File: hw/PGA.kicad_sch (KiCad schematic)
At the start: 17 parts, among them U1401 MAX9939AUB+T

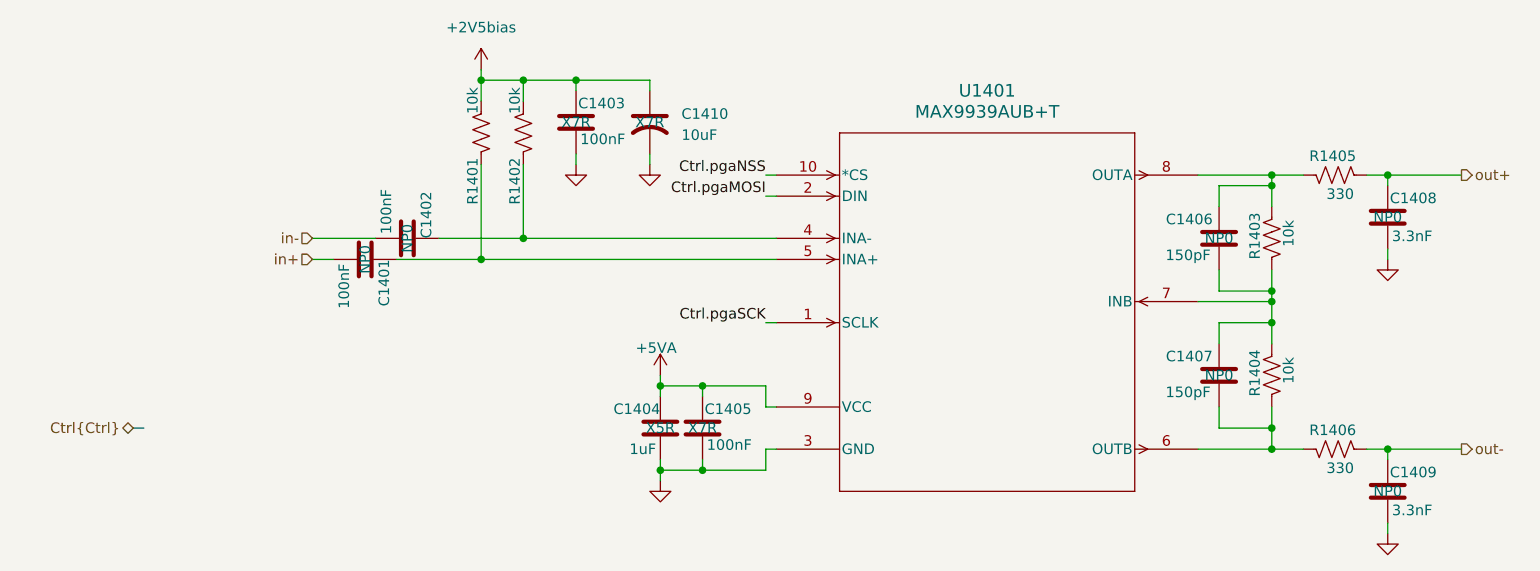
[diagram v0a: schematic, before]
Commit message: Added support for four audio serial links from AK5578 codec to STM32H753, each with 22 ohm series R and I put series R in the clock outputs from STM32 toward AK5578 as well. Reannotated.
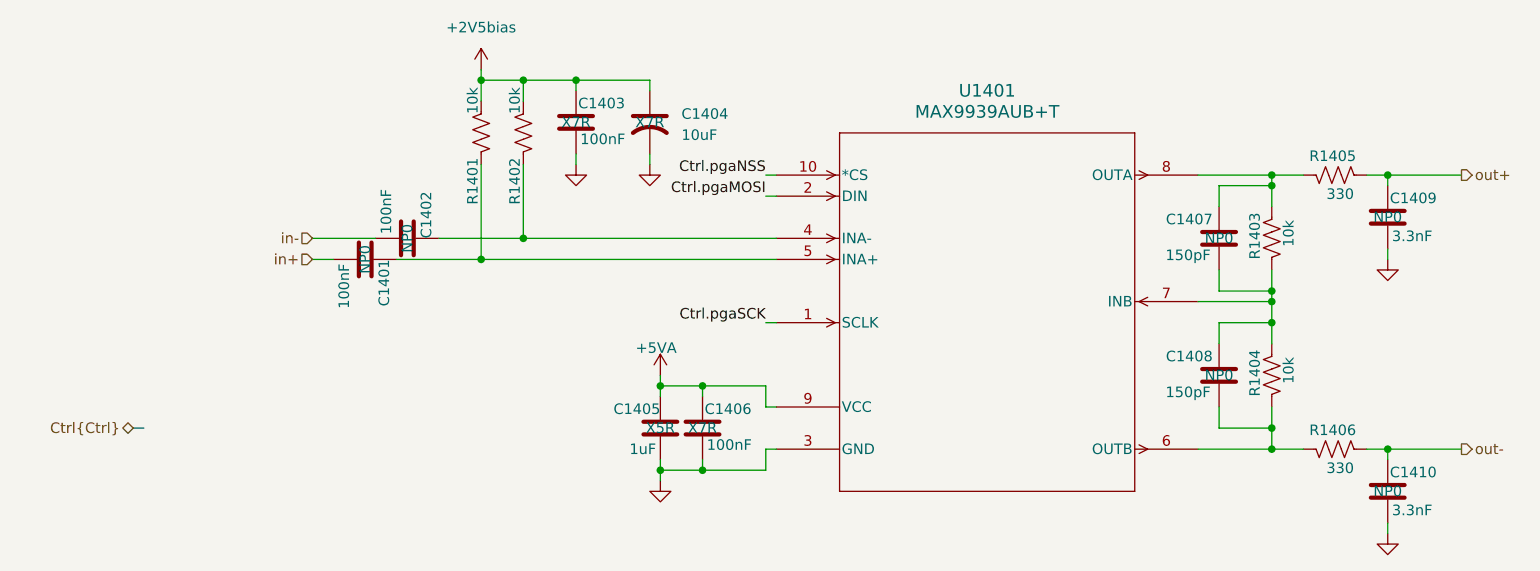
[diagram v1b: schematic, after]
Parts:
- renumbered C1410 to C1404, C1404 to C1405, C1405 to C1406, C1406 to C1407, C1407 to C1408, C1408 to C1409, C1409 to C1410

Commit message: Checkpoint before crazy script screws my files up (again)
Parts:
- renumbered C1401 to C1405, C1402 to C1407, C1403 to C1410, C1404 to C1411, C1405 to C1412, C1406 to C1413, C1407 to C1418, C1408 to C1419, C1409 to C1422, C1410 to C1423, R1401 to R1402, R1402 to R1405, R1403 to R1411, R1404 to R1412, R1405 to R1413, R1406 to R1414
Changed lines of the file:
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@@
 		(on_board yes)
 		(dnp no)
-		(property "Reference" "R1403"
+		(property "Reference" "R1411"
 			(at 164.338 78.74 90)
 			(effects
@@
 				)
 				(path "/8ae46c04-d01a-4756-8774-512b694bfaff/0ee31834-a2c3-474b-9f7c-c9b4f3cadb3f/104f4ab4-5f9d-46b7-aa11-a9b548b73874/5ffcf0e7-51e5-47a9-8fef-78cb8699aff9"
-					(reference "R1403")
+					(reference "R1411")
 					(unit 1)
 				)
@@
 		(on_board yes)
 		(dnp no)
-		(property "Reference" "C1409"
+		(property "Reference" "C1422"
 			(at 180.594 71.374 0)
 			(effects
@@
 				)
 				(path "/8ae46c04-d01a-4756-8774-512b694bfaff/0ee31834-a2c3-474b-9f7c-c9b4f3cadb3f/104f4ab4-5f9d-46b7-aa11-a9b548b73874/5ffcf0e7-51e5-47a9-8fef-78cb8699aff9"
-					(reference "C1409")
+					(reference "C1422")
 					(unit 1)
 				)
@@
 		(on_board yes)
 		(dnp no)
-		(property "Reference" "R1406"
+		(property "Reference" "R1414"
 			(at 176.53 99.314 90)
 			(effects
@@
 				)
 				(path "/8ae46c04-d01a-4756-8774-512b694bfaff/0ee31834-a2c3-474b-9f7c-c9b4f3cadb3f/104f4ab4-5f9d-46b7-aa11-a9b548b73874/5ffcf0e7-51e5-47a9-8fef-78cb8699aff9"
-					(reference "R1406")
+					(reference "R1414")
 					(unit 1)
 				)
@@
 		(dnp no)
 		(fields_autoplaced yes)
-		(property "Reference" "#PWR01405"
+		(property "Reference" "#PWR01417"
 			(at 92.71 111.76 0)
 			(effects
@@
 				)
 				(path "/8ae46c04-d01a-4756-8774-512b694bfaff/0ee31834-a2c3-474b-9f7c-c9b4f3cadb3f/104f4ab4-5f9d-46b7-aa11-a9b548b73874/5ffcf0e7-51e5-47a9-8fef-78cb8699aff9"
-					(reference "#PWR01405")
+					(reference "#PWR01417")
 					(unit 1)
 				)
@@
 		(on_board yes)
 		(dnp no)
-		(property "Reference" "C1407"
+		(property "Reference" "C1418"
 			(at 159.258 73.914 0)
 			(effects
@@
 				)
 				(path "/8ae46c04-d01a-4756-8774-512b694bfaff/0ee31834-a2c3-474b-9f7c-c9b4f3cadb3f/104f4ab4-5f9d-46b7-aa11-a9b548b73874/5ffcf0e7-51e5-47a9-8fef-78cb8699aff9"
-					(reference "C1407")
+					(reference "C1418")
 					(unit 1)
 				)
@@
 		(on_board yes)
 		(dnp no)
-		(property "Reference" "C1408"
+		(property "Reference" "C1419"
 			(at 159.258 90.424 0)
 			(effects
@@
 				)
 				(path "/8ae46c04-d01a-4756-8774-512b694bfaff/0ee31834-a2c3-474b-9f7c-c9b4f3cadb3f/104f4ab4-5f9d-46b7-aa11-a9b548b73874/5ffcf0e7-51e5-47a9-8fef-78cb8699aff9"
-					(reference "C1408")
+					(reference "C1419")
 					(unit 1)
 				)
@@
 		(on_board yes)
 		(dnp no)
-		(property "Reference" "C1410"
+		(property "Reference" "C1423"
 			(at 180.594 104.394 0)
 			(effects
@@
 				)
 				(path "/8ae46c04-d01a-4756-8774-512b694bfaff/0ee31834-a2c3-474b-9f7c-c9b4f3cadb3f/104f4ab4-5f9d-46b7-aa11-a9b548b73874/5ffcf0e7-51e5-47a9-8fef-78cb8699aff9"
-					(reference "C1410")
+					(reference "C1423")
 					(unit 1)
 				)
@@
 		(on_board yes)
 		(dnp no)
-		(property "Reference" "R1401"
+		(property "Reference" "R1402"
 			(at 70.104 72.136 90)
 			(effects
@@
 				)
 				(path "/8ae46c04-d01a-4756-8774-512b694bfaff/0ee31834-a2c3-474b-9f7c-c9b4f3cadb3f/104f4ab4-5f9d-46b7-aa11-a9b548b73874/5ffcf0e7-51e5-47a9-8fef-78cb8699aff9"
-					(reference "R1401")
+					(reference "R1402")
 					(unit 1)
 				)
@@
 		(dnp no)
 		(fields_autoplaced yes)
-		(property "Reference" "#PWR01401"
+		(property "Reference" "#PWR01411"
 			(at 71.12 59.69 0)
 			(effects
@@
 				)
 				(path "/8ae46c04-d01a-4756-8774-512b694bfaff/0ee31834-a2c3-474b-9f7c-c9b4f3cadb3f/104f4ab4-5f9d-46b7-aa11-a9b548b73874/5ffcf0e7-51e5-47a9-8fef-78cb8699aff9"
-					(reference "#PWR01401")
+					(reference "#PWR01411")
 					(unit 1)
 				)
@@
 		(dnp no)
 		(fields_autoplaced yes)
-		(property "Reference" "#PWR01403"
+		(property "Reference" "#PWR01415"
 			(at 91.44 73.66 0)
 			(effects
@@
 				)
 				(path "/8ae46c04-d01a-4756-8774-512b694bfaff/0ee31834-a2c3-474b-9f7c-c9b4f3cadb3f/104f4ab4-5f9d-46b7-aa11-a9b548b73874/5ffcf0e7-51e5-47a9-8fef-78cb8699aff9"
-					(reference "#PWR01403")
+					(reference "#PWR01415")
 					(unit 1)
 				)
@@
 		(on_board yes)
 		(dnp no)
-		(property "Reference" "R1404"
+		(property "Reference" "R1412"
 			(at 164.338 95.25 90)
 			(effects
@@
 				)
 				(path "/8ae46c04-d01a-4756-8774-512b694bfaff/0ee31834-a2c3-474b-9f7c-c9b4f3cadb3f/104f4ab4-5f9d-46b7-aa11-a9b548b73874/5ffcf0e7-51e5-47a9-8fef-78cb8699aff9"
-					(reference "R1404")
+					(reference "R1412")
 					(unit 1)
 				)
@@
 		(on_board yes)
 		(dnp no)
-		(property "Reference" "C1406"
+		(property "Reference" "C1413"
 			(at 98.044 96.774 0)
 			(effects
@@
 				)
 				(path "/8ae46c04-d01a-4756-8774-512b694bfaff/0ee31834-a2c3-474b-9f7c-c9b4f3cadb3f/104f4ab4-5f9d-46b7-aa11-a9b548b73874/5ffcf0e7-51e5-47a9-8fef-78cb8699aff9"
-					(reference "C1406")
+					(reference "C1413")
 					(unit 1)
 				)
@@
 		(on_board yes)
 		(dnp no)
-		(property "Reference" "C1402"
+		(property "Reference" "C1407"
 			(at 64.516 76.2 0)
 			(effects
@@
 				)
 				(path "/8ae46c04-d01a-4756-8774-512b694bfaff/0ee31834-a2c3-474b-9f7c-c9b4f3cadb3f/104f4ab4-5f9d-46b7-aa11-a9b548b73874/5ffcf0e7-51e5-47a9-8fef-78cb8699aff9"
-					(reference "C1402")
+					(reference "C1407")
 					(unit 1)
 				)
@@
 		(dnp no)
 		(fields_autoplaced yes)
-		(property "Reference" "#PWR01402"
+		(property "Reference" "#PWR01413"
 			(at 82.55 73.66 0)
 			(effects
@@
 				)
 				(path "/8ae46c04-d01a-4756-8774-512b694bfaff/0ee31834-a2c3-474b-9f7c-c9b4f3cadb3f/104f4ab4-5f9d-46b7-aa11-a9b548b73874/5ffcf0e7-51e5-47a9-8fef-78cb8699aff9"
-					(reference "#PWR01402")
+					(reference "#PWR01413")
 					(unit 1)
 				)
@@
 		(on_board yes)
 		(dnp no)
-		(property "Reference" "#PWR01404"
+		(property "Reference" "#PWR01416"
 			(at 92.71 96.52 0)
 			(effects
@@
 				)
 				(path "/8ae46c04-d01a-4756-8774-512b694bfaff/0ee31834-a2c3-474b-9f7c-c9b4f3cadb3f/104f4ab4-5f9d-46b7-aa11-a9b548b73874/5ffcf0e7-51e5-47a9-8fef-78cb8699aff9"
-					(reference "#PWR01404")
+					(reference "#PWR01416")
 					(unit 1)
 				)
@@
 		(dnp no)
 		(fields_autoplaced yes)
-		(property "Reference" "C1404"
+		(property "Reference" "C1411"
 			(at 95.25 61.2139 0)
 			(effects
@@
 				)
 				(path "/8ae46c04-d01a-4756-8774-512b694bfaff/0ee31834-a2c3-474b-9f7c-c9b4f3cadb3f/104f4ab4-5f9d-46b7-aa11-a9b548b73874/5ffcf0e7-51e5-47a9-8fef-78cb8699aff9"
-					(reference "C1404")
+					(reference "C1411")
 					(unit 1)
 				)
@@
 		(on_board yes)
 		(dnp no)
-		(property "Reference" "R1405"
+		(property "Reference" "R1413"
 			(at 176.53 66.294 90)
 			(effects
@@
 				)
 				(path "/8ae46c04-d01a-4756-8774-512b694bfaff/0ee31834-a2c3-474b-9f7c-c9b4f3cadb3f/104f4ab4-5f9d-46b7-aa11-a9b548b73874/5ffcf0e7-51e5-47a9-8fef-78cb8699aff9"
-					(reference "R1405")
+					(reference "R1413")
 					(unit 1)
 				)
@@
 		(on_board yes)
 		(dnp no)
-		(property "Reference" "C1401"
+		(property "Reference" "C1405"
 			(at 59.436 78.74 0)
 			(effects
@@
 				)
 				(path "/8ae46c04-d01a-4756-8774-512b694bfaff/0ee31834-a2c3-474b-9f7c-c9b4f3cadb3f/104f4ab4-5f9d-46b7-aa11-a9b548b73874/5ffcf0e7-51e5-47a9-8fef-78cb8699aff9"
-					(reference "C1401")
+					(reference "C1405")
 					(unit 1)
 				)
@@
 		(dnp no)
 		(fields_autoplaced yes)
-		(property "Reference" "#PWR01406"
+		(property "Reference" "#PWR01425"
 			(at 180.34 85.09 0)
 			(effects
@@
 				)
 				(path "/8ae46c04-d01a-4756-8774-512b694bfaff/0ee31834-a2c3-474b-9f7c-c9b4f3cadb3f/104f4ab4-5f9d-46b7-aa11-a9b548b73874/5ffcf0e7-51e5-47a9-8fef-78cb8699aff9"
-					(reference "#PWR01406")
+					(reference "#PWR01425")
 					(unit 1)
 				)
@@
 		(on_board yes)
 		(dnp no)
-		(property "Reference" "C1405"
+		(property "Reference" "C1412"
 			(at 92.71 96.774 0)
 			(effects
@@
 				)
 				(path "/8ae46c04-d01a-4756-8774-512b694bfaff/0ee31834-a2c3-474b-9f7c-c9b4f3cadb3f/104f4ab4-5f9d-46b7-aa11-a9b548b73874/5ffcf0e7-51e5-47a9-8fef-78cb8699aff9"
-					(reference "C1405")
+					(reference "C1412")
 					(unit 1)
 				)
@@
 		(on_board yes)
 		(dnp no)
-		(property "Reference" "R1402"
+		(property "Reference" "R1405"
 			(at 75.184 72.136 90)
 			(effects
@@
 				)
 				(path "/8ae46c04-d01a-4756-8774-512b694bfaff/0ee31834-a2c3-474b-9f7c-c9b4f3cadb3f/104f4ab4-5f9d-46b7-aa11-a9b548b73874/5ffcf0e7-51e5-47a9-8fef-78cb8699aff9"
-					(reference "R1402")
+					(reference "R1405")
 					(unit 1)
 				)
@@
 		(dnp no)
 		(fields_autoplaced yes)
-		(property "Reference" "#PWR01407"
+		(property "Reference" "#PWR01426"
 			(at 180.34 118.11 0)
 			(effects
@@
 				)
 				(path "/8ae46c04-d01a-4756-8774-512b694bfaff/0ee31834-a2c3-474b-9f7c-c9b4f3cadb3f/104f4ab4-5f9d-46b7-aa11-a9b548b73874/5ffcf0e7-51e5-47a9-8fef-78cb8699aff9"
-					(reference "#PWR01407")
+					(reference "#PWR01426")
 					(unit 1)
 				)
@@
 		(on_board yes)
 		(dnp no)
-		(property "Reference" "C1403"
+		(property "Reference" "C1410"
 			(at 82.804 59.944 0)
 			(effects
@@
 				)
 				(path "/8ae46c04-d01a-4756-8774-512b694bfaff/0ee31834-a2c3-474b-9f7c-c9b4f3cadb3f/104f4ab4-5f9d-46b7-aa11-a9b548b73874/5ffcf0e7-51e5-47a9-8fef-78cb8699aff9"
-					(reference "C1403")
+					(reference "C1410")
 					(unit 1)
 				)

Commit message: Ready to buy the first BOM parts for DVT1 PCBs that have small solder bridge issues for USB-C connector
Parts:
- C1422, C1423: working-voltage 25V -> 50V
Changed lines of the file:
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@@
 			)
 		)
-		(property "working-voltage" "25V"
+		(property "working-voltage" "50V"
 			(at 180.34 73.66 0)
 			(effects
@@
 			)
 		)
-		(property "working-voltage" "25V"
-			(at 180.34 106.68 0)
-			(effects
+		(property "working-voltage" "50V"
+			(at 180.34 106.68 0)
+			(effects

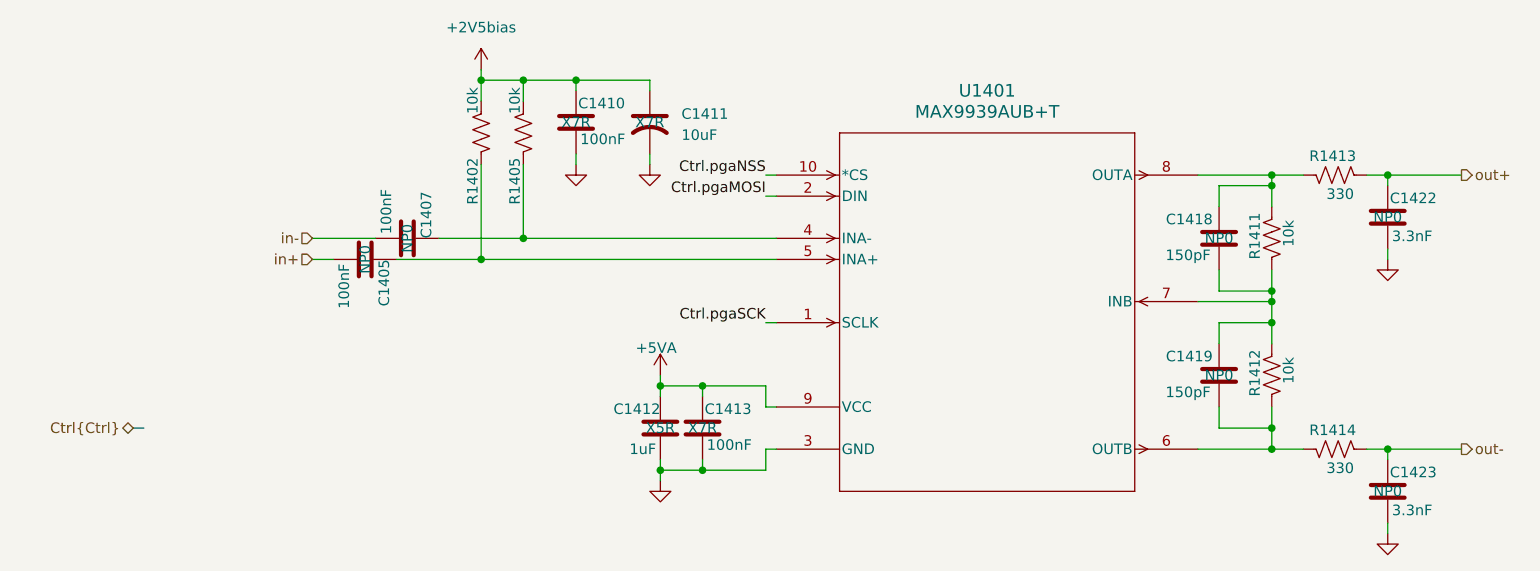
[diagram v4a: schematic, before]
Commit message: Add filter-tester board project
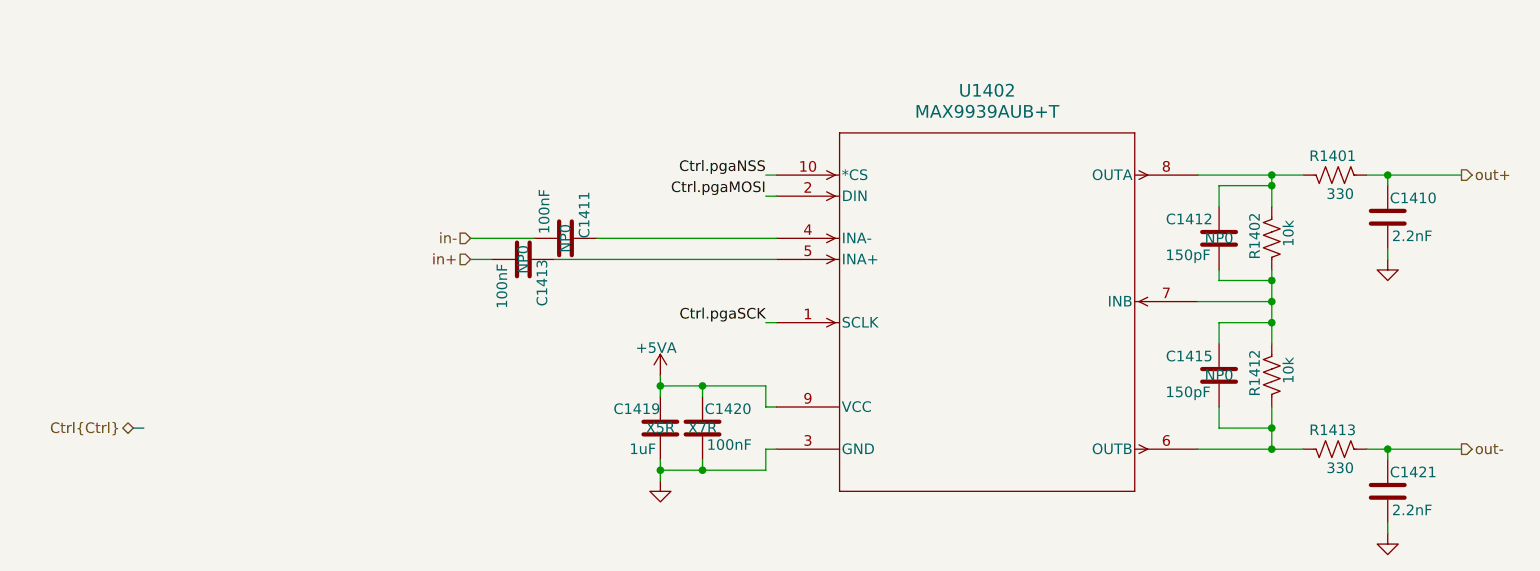
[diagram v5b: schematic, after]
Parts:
- removed C1410: 100nF, Capacitor_SMD:C_0603_1608Metric, symbol Device:C
- removed C1411: 10uF, Capacitor_SMD:C_0603_1608Metric, symbol Device:C_US
- removed R1402, R1405: 10k, Resistor_SMD:R_0402_1005Metric, symbol Device:R_US
- C1410: renamed from C1422; value 3.3nF -> 2.2nF; LCSC_PN C107048 -> (none); MPN C1608C0G1H332J080AE -> (none); Manufacturer TDK -> (none); Mouser_PN 810-C1608C0G1H332J08 -> (none); cap-type NP0 -> (none)
- C1420: renamed from C1413; footprint Capacitor_SMD:C_0603_1608Metric -> Capacitor_SMD:C_0402_1005Metric
- C1421: renamed from C1423; value 3.3nF -> 2.2nF; LCSC_PN C107048 -> (none); MPN C1608C0G1H332J080AE -> (none); Manufacturer TDK -> (none); Mouser_PN 810-C1608C0G1H332J08 -> (none); cap-type NP0 -> (none)
- renumbered C1407 to C1411, C1418 to C1412, C1405 to C1413, C1419 to C1415, C1412 to C1419, R1413 to R1401, R1411 to R1402, R1414 to R1413, U1401 to U1402
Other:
- moved on the sheet: C1411, C1413
